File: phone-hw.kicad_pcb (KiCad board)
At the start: 2 copper layers, 66 x 100 mm, 76 parts, among them J1 USB_C_Receptacle_USB2.0, J2 Micro_SD_Card, J4 SIM_Card, J5 BATT+, J6 BATT-, Q1 BC847BLT3G, Q2 S9015, Q3 RU8205G, SW1 SW_Push, SW2 SW_Push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

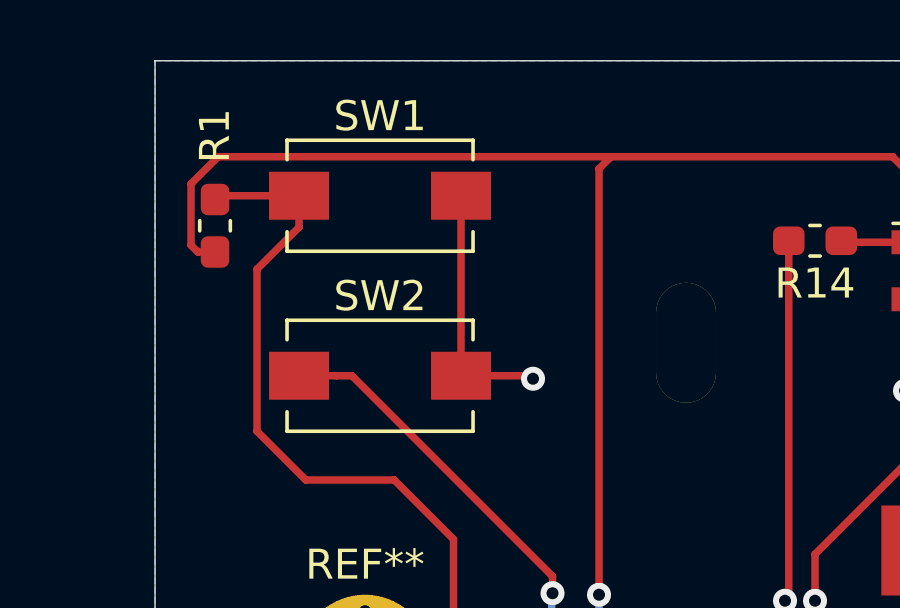
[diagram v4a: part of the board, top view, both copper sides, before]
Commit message: add names of buttons to silkscreen
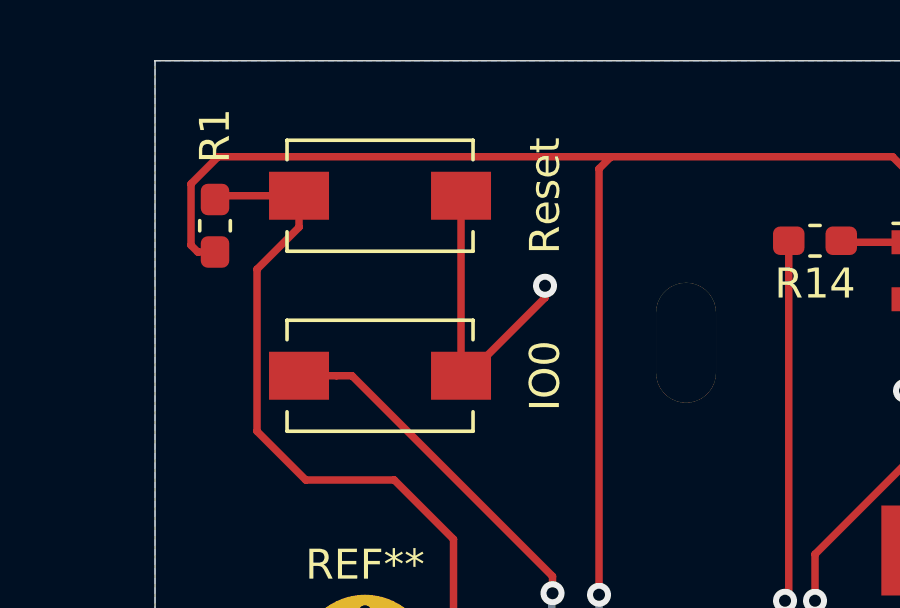
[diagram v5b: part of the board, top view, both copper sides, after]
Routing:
- net GND_OUT: track 274.1 -> 276.0 mm
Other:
- board text added: "IO0"
- board text added: "Reset"
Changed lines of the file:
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@@
   (general
     (thickness 1.6)
-    (drawings 11)
-    (tracks 1572)
+    (drawings 13)
+    (tracks 1573)
     (zones 0)
     (modules 76)
@@
     (descr "Light Touch Switch, https://industrial.panasonic.com/cdbs/www-data/pdf/ATK0000/ATK0000CE7.pdf")
     (attr smd)
-    (fp_text reference SW1 (at 0 -2.65) (layer F.SilkS)
+    (fp_text reference SW1 (at 0 -2.65) (layer F.SilkS) hide
       (effects (font (size 1 1) (thickness 0.15)))
     )
@@
     (descr "Light Touch Switch, https://industrial.panasonic.com/cdbs/www-data/pdf/ATK0000/ATK0000CE7.pdf")
     (attr smd)
-    (fp_text reference SW2 (at 0 -2.65) (layer F.SilkS)
+    (fp_text reference SW2 (at 0 -2.65) (layer F.SilkS) hide
       (effects (font (size 1 1) (thickness 0.15)))
     )
@@
     )
   )
+  (gr_text IO0 (at 33 30.5 90) (layer F.SilkS)
+    (effects (font (size 1 1) (thickness 0.15)))
+  )
+  (gr_text Reset (at 33 24.5 90) (layer F.SilkS)
+    (effects (font (size 1 1) (thickness 0.15)))
+  )
   (gr_text +BATT (at 70.75 114.5 270) (layer B.SilkS)
     (effects (font (size 1 1) (thickness 0.15)) (justify left mirror))
@@
   (segment (start 24.981642 70.481642) (end 25 70.5) (width 0.25) (layer B.Cu) (net 1))
   (segment (start 24.981642 67.981642) (end 24.981642 70.481642) (width 0.25) (layer B.Cu) (net 1))
-  (via (at 32.6 30.6) (size 0.8) (drill 0.4) (layers F.Cu B.Cu) (net 1))
-  (segment (start 32.5 30.5) (end 32.6 30.6) (width 0.25) (layer F.Cu) (net 1))
-  (segment (start 30.2 30.5) (end 32.5 30.5) (width 0.25) (layer F.Cu) (net 1))
   (segment (start 55.75 33.125) (end 55.75 34) (width 0.25) (layer F.Cu) (net 1))
   (segment (start 55.825001 33.049999) (end 55.75 33.125) (width 0.25) (layer F.Cu) (net 1))
@@
   (segment (start 71.88 65.12) (end 71.9 65.1) (width 0.25) (layer F.Cu) (net 1))
   (segment (start 70.075 65.12) (end 71.88 65.12) (width 0.25) (layer F.Cu) (net 1))
+  (segment (start 33 27.9) (end 33 27.5) (width 0.25) (layer F.Cu) (net 1))
+  (segment (start 30.4 30.5) (end 33 27.9) (width 0.25) (layer F.Cu) (net 1))
+  (via (at 33 27.5) (size 0.8) (drill 0.4) (layers F.Cu B.Cu) (net 1))
+  (segment (start 30.2 30.5) (end 30.4 30.5) (width 0.25) (layer F.Cu) (net 1))
   (segment (start 68.65 71.5) (end 68.65 69.25) (width 0.25) (layer F.Cu) (net 2))
   (segment (start 68.65 69.25) (end 68.65 68.75) (width 0.25) (layer F.Cu) (net 2))
